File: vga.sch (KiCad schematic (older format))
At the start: 1 part

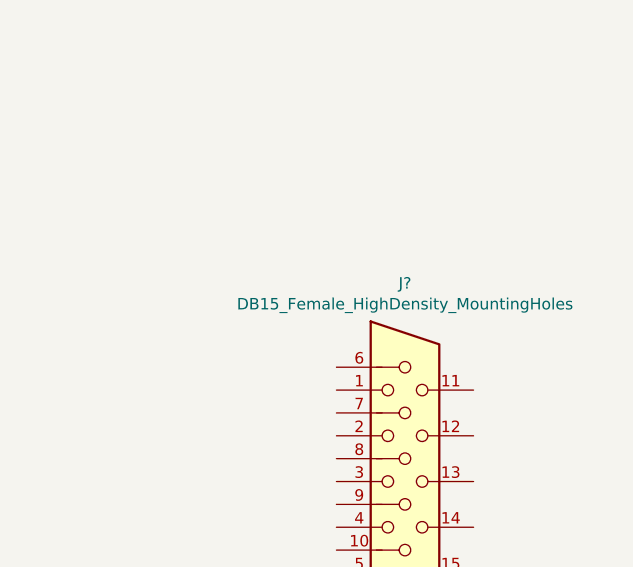
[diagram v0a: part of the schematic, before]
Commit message: Added some footprints. Basic board outline.
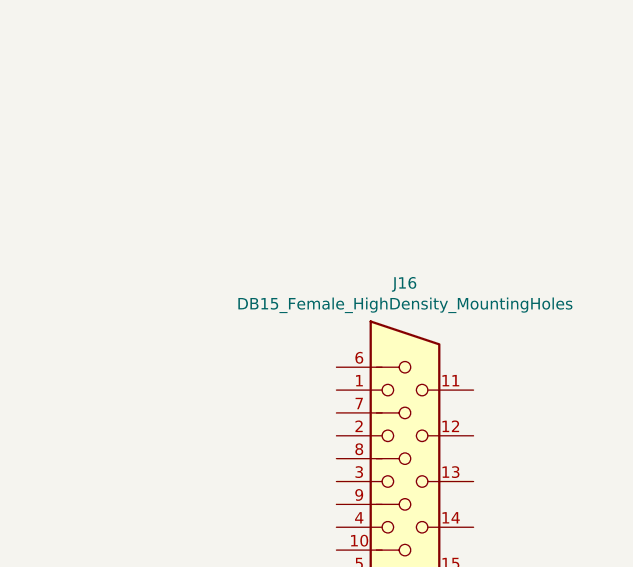
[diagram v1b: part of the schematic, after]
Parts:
- gave numbers to parts that had none: 1
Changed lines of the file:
@@
 $Descr A4 11693 8268
 encoding utf-8
-Sheet 5 11
+Sheet 11 11
 Title "Neotron 32K"
 Date "2019-12-08"
@@
 P 5500 4250
 AR Path="/5DF388AB" Ref="J?"  Part="1"
-AR Path="/5DF25A09/5DF388AB" Ref="J?"  Part="1"
-F 0 "J?" H 5500 5117 50  0000 C CNN
+AR Path="/5DF25A09/5DF388AB" Ref="J16"  Part="1"
+F 0 "J16" H 5500 5117 50  0000 C CNN
 F 1 "DB15_Female_HighDensity_MountingHoles" H 5500 5026 50  0000 C CNN
 F 2 "Connector_Dsub:DSUB-15-HD_Female_Horizontal_P2.29x1.98mm_EdgePinOffset3.03mm_Housed_MountingHolesOffset4.94mm" H 4550 4650 50  0001 C CNN

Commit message: Completed Power, SD, MIDI, Parallel and Joystick sheets.
Switch to sheet based 100x part numbering.
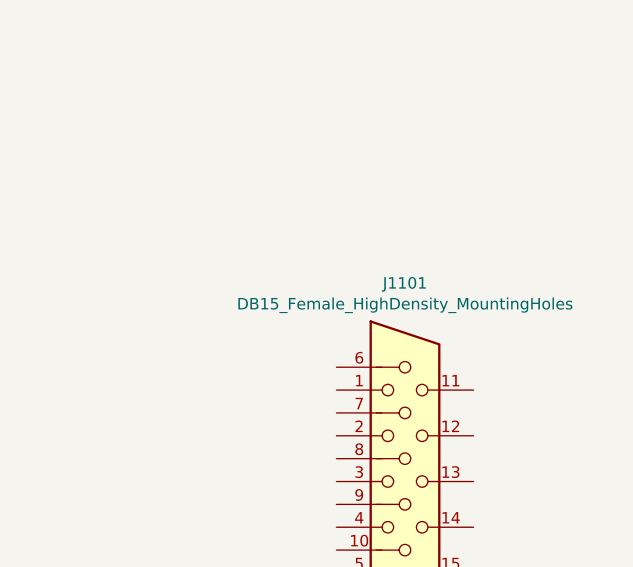
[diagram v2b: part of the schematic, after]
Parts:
- renumbered J16 to J1101
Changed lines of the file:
@@
 P 5500 4250
 AR Path="/5DF388AB" Ref="J?"  Part="1"
-AR Path="/5DF25A09/5DF388AB" Ref="J16"  Part="1"
-F 0 "J16" H 5500 5117 50  0000 C CNN
+AR Path="/5DF25A09/5DF388AB" Ref="J1101"  Part="1"
+F 0 "J1101" H 5500 5117 50  0000 C CNN
 F 1 "DB15_Female_HighDensity_MountingHoles" H 5500 5026 50  0000 C CNN
 F 2 "Connector_Dsub:DSUB-15-HD_Female_Horizontal_P2.29x1.98mm_EdgePinOffset3.03mm_Housed_MountingHolesOffset4.94mm" H 4550 4650 50  0001 C CNN

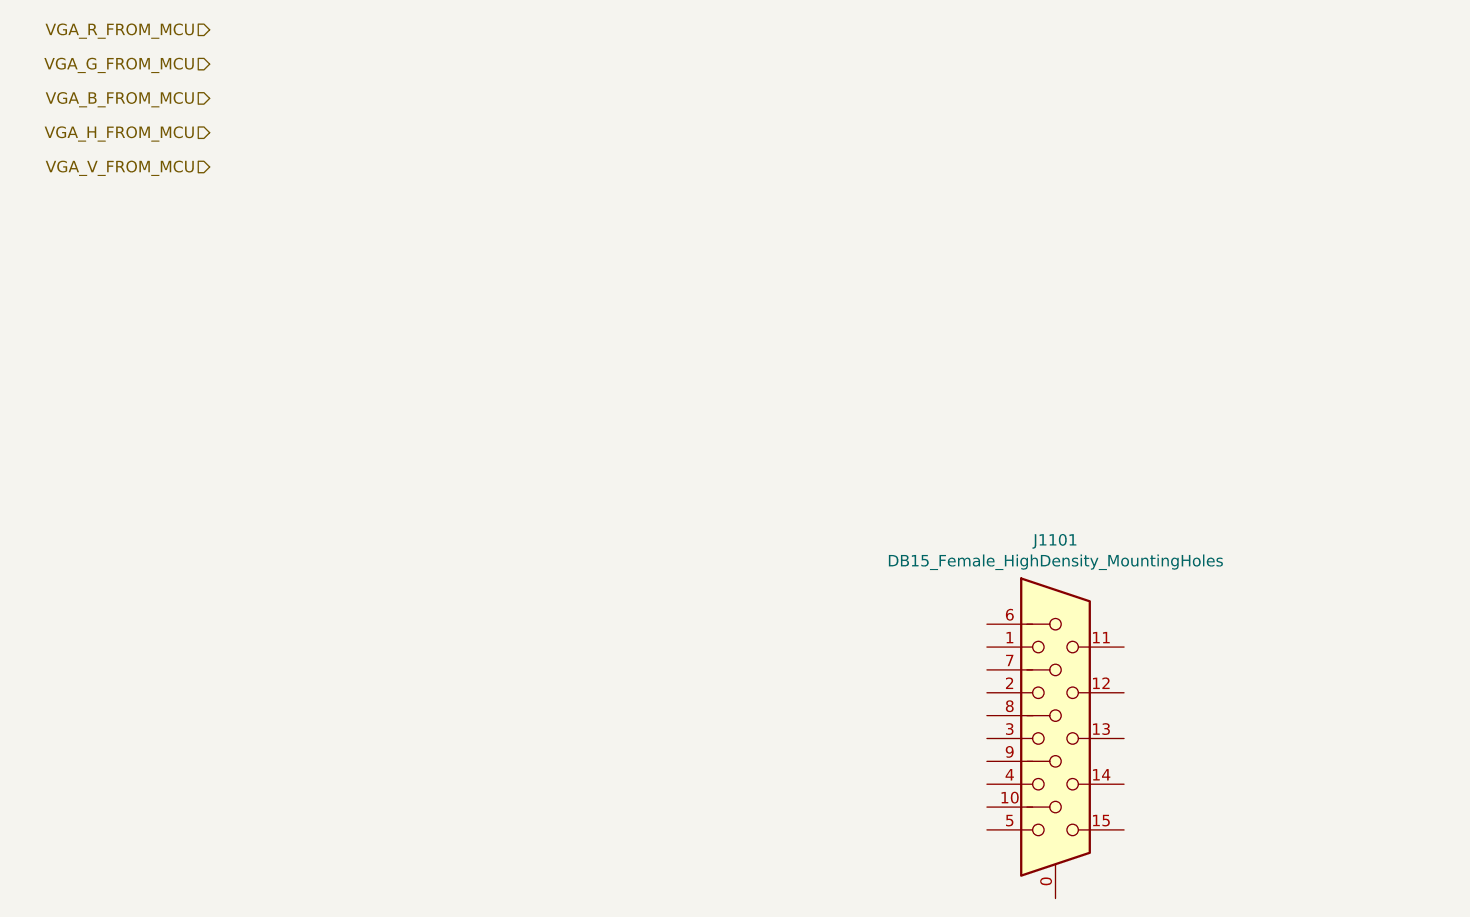
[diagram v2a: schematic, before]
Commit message: Schematic capture draft complete.
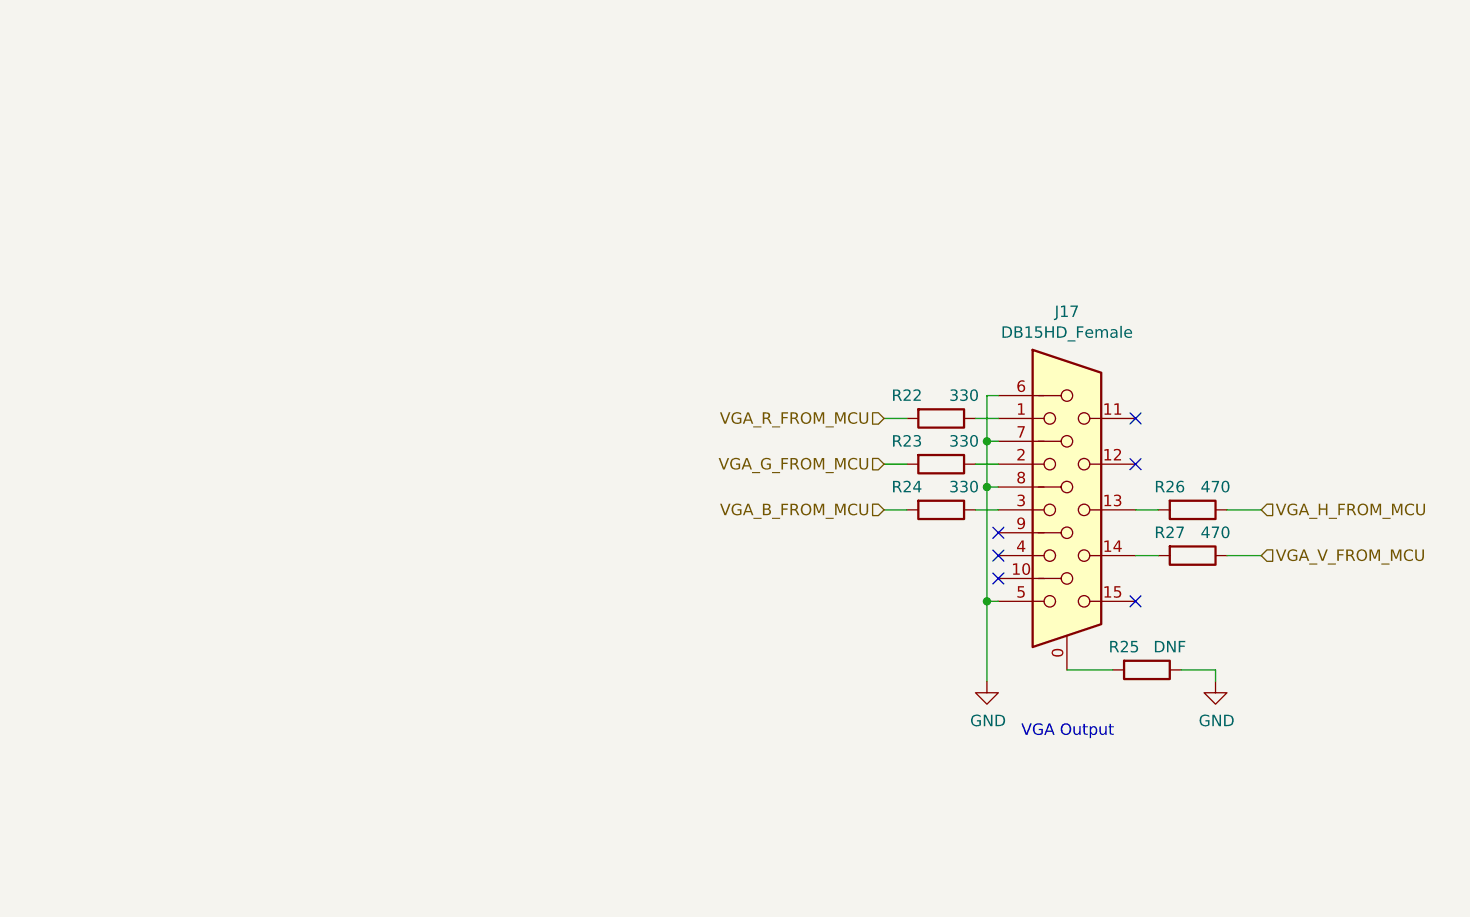
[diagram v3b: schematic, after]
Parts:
- added R22, R23, R24: 330, Resistor_THT:R_Axial_DIN0411_L9.9mm_D3.6mm_P12.70mm_Horizontal, symbol Device:R
- added R25: DNF, Resistor_THT:R_Axial_DIN0411_L9.9mm_D3.6mm_P12.70mm_Horizontal, symbol Device:R
- added R26, R27: 470, Resistor_THT:R_Axial_DIN0411_L9.9mm_D3.6mm_P12.70mm_Horizontal, symbol Device:R
- J17: renamed from J1101; value DB15_Female_HighDensity_MountingHoles -> DB15HD_Female; Digikey (none) -> 609-5180-ND
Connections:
- net VGA_B_FROM_MCU: now also R24.2
- net VGA_G_FROM_MCU: now also R23.2
- net VGA_H_FROM_MCU: now also R26.1
- net VGA_R_FROM_MCU: now also R22.2
- net VGA_V_FROM_MCU: now also R27.1
- net at J17.0: now also R25.2
- net at J17.1: now also R22.1
- net at J17.13: now also R26.2
- net at J17.14: now also R27.2
- net at J17.2: now also R23.1
- net at J17.3: now also R24.1
- net GND: now reaches J17.5
- net GND: now also J17.6, J17.7, J17.8, R25.1
- no-connect marks 0 -> 6
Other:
- note added: "VGA Output"
- moved on the sheet: J17
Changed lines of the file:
@@
 $Descr A4 11693 8268
 encoding utf-8
-Sheet 11 11
-Title "Neotron 32K"
-Date "2019-12-08"
-Rev "0.1"
-Comp "github.com/thejpster"
-Comment1 ""
-Comment2 ""
+Sheet 9 10
+Title "Neotron 32K Main PCB"
+Date "2019-12-15"
+Rev "0.5"
+Comp "github.com/neotron-compute/Neotron-32-Hardware"
+Comment1 "Copyright (c) Jonathan 'theJPster' Pallant"
+Comment2 "CC BY-SA 4.0"
 Comment3 ""
 Comment4 ""
@@
 L Connector:DB15_Female_HighDensity_MountingHoles J?
 U 1 1 5DF388AB
-P 5500 4250
+P 5550 3250
 AR Path="/5DF388AB" Ref="J?"  Part="1"
-AR Path="/5DF25A09/5DF388AB" Ref="J1101"  Part="1"
-F 0 "J1101" H 5500 5117 50  0000 C CNN
-F 1 "DB15_Female_HighDensity_MountingHoles" H 5500 5026 50  0000 C CNN
-F 2 "Connector_Dsub:DSUB-15-HD_Female_Horizontal_P2.29x1.98mm_EdgePinOffset3.03mm_Housed_MountingHolesOffset4.94mm" H 4550 4650 50  0001 C CNN
-F 3 " ~" H 4550 4650 50  0001 C CNN
-	1    5500 4250
+AR Path="/5DF25A09/5DF388AB" Ref="J17"  Part="1"
+F 0 "J17" H 5550 4117 50  0000 C CNN
+F 1 "DB15HD_Female" H 5550 4026 50  0000 C CNN
+F 2 "Connector_Dsub:DSUB-15-HD_Female_Horizontal_P2.29x1.98mm_EdgePinOffset3.03mm_Housed_MountingHolesOffset4.94mm" H 4600 3650 50  0001 C CNN
+F 3 "https://www.amphenol-icc.com/media/wysiwyg/files/drawing/c-cd-0012.pdf" H 4600 3650 50  0001 C CNN
+F 4 "609-5180-ND" H 5550 3250 50  0001 C CNN "Digikey"
+	1    5550 3250
 	1    0    0    -1
 $EndComp
-Text HLabel 1800 1150 0    50   Input ~ 0
+Text HLabel 4750 2850 0    50   Input ~ 0
 VGA_R_FROM_MCU
-Text HLabel 1800 1300 0    50   Input ~ 0
+Text HLabel 4750 3050 0    50   Input ~ 0
 VGA_G_FROM_MCU
-Text HLabel 1800 1450 0    50   Input ~ 0
+Text HLabel 4750 3250 0    50   Input ~ 0
 VGA_B_FROM_MCU
-Text HLabel 1800 1600 0    50   Input ~ 0
+Text HLabel 6400 3250 2    50   Input ~ 0
 VGA_H_FROM_MCU
-Text HLabel 1800 1750 0    50   Input ~ 0
+Text HLabel 6400 3450 2    50   Input ~ 0
 VGA_V_FROM_MCU
+$Comp
+L Device:R R27
+U 1 1 5E020EF6
+P 6100 3450
+F 0 "R27" V 6000 3350 50  0000 C CNN
+F 1 "470" V 6000 3550 50  0000 C CNN
+F 2 "Resistor_THT:R_Axial_DIN0411_L9.9mm_D3.6mm_P12.70mm_Horizontal" V 6030 3450 50  0001 C CNN
+F 3 "~" H 6100 3450 50  0001 C CNN
+	1    6100 3450
+	0    1    1    0
+$EndComp
+$Comp
+L Device:R R26
+U 1 1 5E02143C
+P 6100 3250
+F 0 "R26" V 6000 3150 50  0000 C CNN
+F 1 "470" V 6000 3350 50  0000 C CNN
+F 2 "Resistor_THT:R_Axial_DIN0411_L9.9mm_D3.6mm_P12.70mm_Horizontal" V 6030 3250 50  0001 C CNN
+F 3 "~" H 6100 3250 50  0001 C CNN
+	1    6100 3250
+	0    1    1    0
+$EndComp
+$Comp
+L Device:R R22
+U 1 1 5E021698
+P 5000 2850
+F 0 "R22" V 4900 2700 50  0000 C CNN
+F 1 "330" V 4900 2950 50  0000 C CNN
+F 2 "Resistor_THT:R_Axial_DIN0411_L9.9mm_D3.6mm_P12.70mm_Horizontal" V 4930 2850 50  0001 C CNN
+F 3 "~" H 5000 2850 50  0001 C CNN
+	1    5000 2850
+	0    1    1    0
+$EndComp
+$Comp
+L Device:R R23
+U 1 1 5E021BC3
+P 5000 3050
+F 0 "R23" V 4900 2900 50  0000 C CNN
+F 1 "330" V 4900 3150 50  0000 C CNN
+F 2 "Resistor_THT:R_Axial_DIN0411_L9.9mm_D3.6mm_P12.70mm_Horizontal" V 4930 3050 50  0001 C CNN
+F 3 "~" H 5000 3050 50  0001 C CNN
+	1    5000 3050
+	0    1    1    0
+$EndComp
+$Comp
+L Device:R R24
+U 1 1 5E021E5E
+P 5000 3250
+F 0 "R24" V 4900 3100 50  0000 C CNN
+F 1 "330" V 4900 3350 50  0000 C CNN
+F 2 "Resistor_THT:R_Axial_DIN0411_L9.9mm_D3.6mm_P12.70mm_Horizontal" V 4930 3250 50  0001 C CNN
+F 3 "~" H 5000 3250 50  0001 C CNN
+	1    5000 3250
+	0    1    1    0
+$EndComp
+Wire Wire Line
+	4750 2850 4850 2850
+Wire Wire Line
+	4750 3050 4850 3050
+Wire Wire Line
+	4750 3250 4850 3250
+Wire Wire Line
+	5150 2850 5250 2850
+Wire Wire Line
+	5150 3050 5250 3050
+Wire Wire Line
+	5150 3250 5250 3250
+Wire Wire Line
+	5850 3250 5950 3250
+Wire Wire Line
+	6250 3250 6400 3250
+Wire Wire Line
+	6250 3450 6400 3450
+Wire Wire Line
+	5850 3450 5950 3450
+NoConn ~ 5850 3650
+NoConn ~ 5250 3550
+NoConn ~ 5250 3450
+NoConn ~ 5250 3350
+NoConn ~ 5850 2850
+NoConn ~ 5850 3050
+Wire Wire Line
+	5250 2750 5200 2750
+Wire Wire Line
+	5200 2750 5200 2950
+Wire Wire Line
+	5200 2950 5250 2950
+Connection ~ 5200 2950
+Wire Wire Line
+	5200 2950 5200 3150
+Wire Wire Line
+	5200 3150 5250 3150
+Connection ~ 5200 3150
+Wire Wire Line
+	5200 3150 5200 3650
+Wire Wire Line
+	5200 3650 5250 3650
+Connection ~ 5200 3650
+$Comp
+L power:GND #PWR066
+U 1 1 5E02516A
+P 5200 4000
+F 0 "#PWR066" H 5200 3750 50  0001 C CNN
+F 1 "GND" H 5205 3827 50  0000 C CNN
+F 2 "" H 5200 4000 50  0001 C CNN
+F 3 "" H 5200 4000 50  0001 C CNN
+	1    5200 4000
+	1    0    0    -1
+$EndComp
+Text Notes 5350 4250 0    50   ~ 0
+VGA Output
+$Comp
+L Device:R R25
+U 1 1 5E3BC4C1
+P 5900 3950
+F 0 "R25" V 5800 3850 50  0000 C CNN
+F 1 "DNF" V 5800 4050 50  0000 C CNN
+F 2 "Resistor_THT:R_Axial_DIN0411_L9.9mm_D3.6mm_P12.70mm_Horizontal" V 5830 3950 50  0001 C CNN
+F 3 "~" H 5900 3950 50  0001 C CNN
+	1    5900 3950
+	0    1    1    0
+$EndComp
+$Comp
+L power:GND #PWR067
+U 1 1 5E3BC797
+P 6200 4000
+F 0 "#PWR067" H 6200 3750 50  0001 C CNN
+F 1 "GND" H 6205 3827 50  0000 C CNN
+F 2 "" H 6200 4000 50  0001 C CNN
+F 3 "" H 6200 4000 50  0001 C CNN
+	1    6200 4000
+	1    0    0    -1
+$EndComp
+Wire Wire Line
+	5550 3950 5750 3950
+Wire Wire Line
+	6050 3950 6200 3950
+Wire Wire Line
+	6200 3950 6200 4000
+Wire Wire Line
+	5200 3650 5200 4000
 $EndSCHEMATC

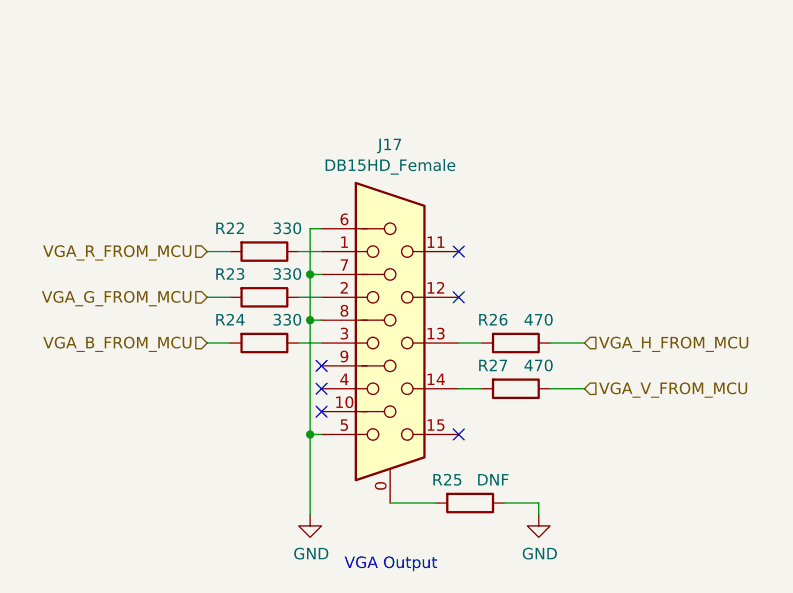
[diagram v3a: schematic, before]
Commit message: Tidied up Atmega power. Added page titles.
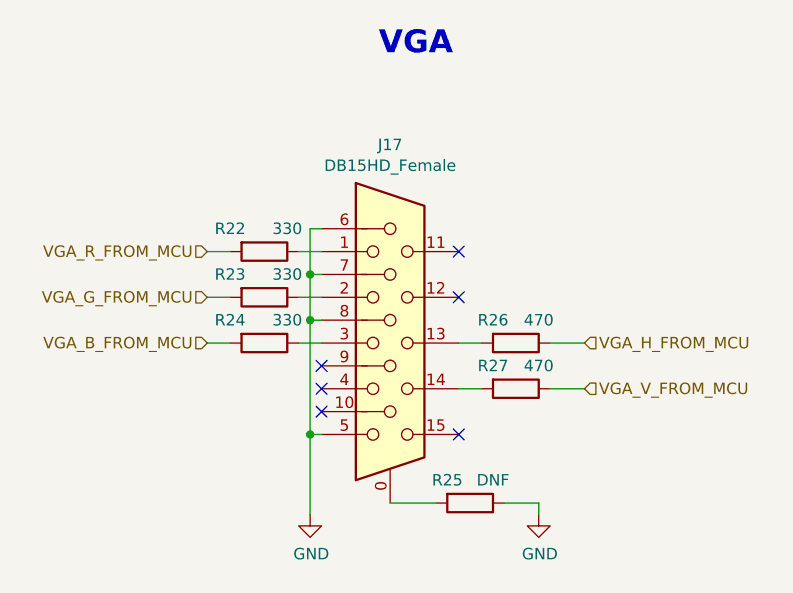
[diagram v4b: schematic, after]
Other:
- note added: "VGA"
- note removed: "VGA Output"
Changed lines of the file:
@@
 Sheet 9 10
 Title "Neotron 32K Main PCB"
-Date "2019-12-15"
-Rev "0.5"
+Date "2019-12-16"
+Rev "0.6"
 Comp "github.com/neotron-compute/Neotron-32-Hardware"
 Comment1 "Copyright (c) Jonathan 'theJPster' Pallant"
@@
 	1    0    0    -1
 $EndComp
-Text Notes 5350 4250 0    50   ~ 0
-VGA Output
 $Comp
 L Device:R R25
@@
 Wire Wire Line
 	5200 3650 5200 4000
+Text Notes 5500 2000 0    100  ~ 20
+VGA
 $EndSCHEMATC

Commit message: Updated footprints: ) Swapped RS-232 DE9 for IDC header. ) Large caps are radial electrolytics. ) Made resistors a little smaller.
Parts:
- R22, R23, R24, R25, R26, R27: footprint Resistor_THT:R_Axial_DIN0411_L9.9mm_D3.6mm_P12.70mm_Horizontal -> Resistor_THT:R_Axial_DIN0207_L6.3mm_D2.5mm_P10.16mm_Horizontal
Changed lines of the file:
@@
 F 0 "R27" V 6000 3350 50  0000 C CNN
 F 1 "470" V 6000 3550 50  0000 C CNN
-F 2 "Resistor_THT:R_Axial_DIN0411_L9.9mm_D3.6mm_P12.70mm_Horizontal" V 6030 3450 50  0001 C CNN
+F 2 "Resistor_THT:R_Axial_DIN0207_L6.3mm_D2.5mm_P10.16mm_Horizontal" V 6030 3450 50  0001 C CNN
 F 3 "~" H 6100 3450 50  0001 C CNN
 	1    6100 3450
@@
 F 0 "R26" V 6000 3150 50  0000 C CNN
 F 1 "470" V 6000 3350 50  0000 C CNN
-F 2 "Resistor_THT:R_Axial_DIN0411_L9.9mm_D3.6mm_P12.70mm_Horizontal" V 6030 3250 50  0001 C CNN
+F 2 "Resistor_THT:R_Axial_DIN0207_L6.3mm_D2.5mm_P10.16mm_Horizontal" V 6030 3250 50  0001 C CNN
 F 3 "~" H 6100 3250 50  0001 C CNN
 	1    6100 3250
@@
 F 0 "R22" V 4900 2700 50  0000 C CNN
 F 1 "330" V 4900 2950 50  0000 C CNN
-F 2 "Resistor_THT:R_Axial_DIN0411_L9.9mm_D3.6mm_P12.70mm_Horizontal" V 4930 2850 50  0001 C CNN
+F 2 "Resistor_THT:R_Axial_DIN0207_L6.3mm_D2.5mm_P10.16mm_Horizontal" V 4930 2850 50  0001 C CNN
 F 3 "~" H 5000 2850 50  0001 C CNN
 	1    5000 2850
@@
 F 0 "R23" V 4900 2900 50  0000 C CNN
 F 1 "330" V 4900 3150 50  0000 C CNN
-F 2 "Resistor_THT:R_Axial_DIN0411_L9.9mm_D3.6mm_P12.70mm_Horizontal" V 4930 3050 50  0001 C CNN
+F 2 "Resistor_THT:R_Axial_DIN0207_L6.3mm_D2.5mm_P10.16mm_Horizontal" V 4930 3050 50  0001 C CNN
 F 3 "~" H 5000 3050 50  0001 C CNN
 	1    5000 3050
@@
 F 0 "R24" V 4900 3100 50  0000 C CNN
 F 1 "330" V 4900 3350 50  0000 C CNN
-F 2 "Resistor_THT:R_Axial_DIN0411_L9.9mm_D3.6mm_P12.70mm_Horizontal" V 4930 3250 50  0001 C CNN
+F 2 "Resistor_THT:R_Axial_DIN0207_L6.3mm_D2.5mm_P10.16mm_Horizontal" V 4930 3250 50  0001 C CNN
 F 3 "~" H 5000 3250 50  0001 C CNN
 	1    5000 3250
@@
 F 0 "R25" V 5800 3850 50  0000 C CNN
 F 1 "DNF" V 5800 4050 50  0000 C CNN
-F 2 "Resistor_THT:R_Axial_DIN0411_L9.9mm_D3.6mm_P12.70mm_Horizontal" V 5830 3950 50  0001 C CNN
+F 2 "Resistor_THT:R_Axial_DIN0207_L6.3mm_D2.5mm_P10.16mm_Horizontal" V 5830 3950 50  0001 C CNN
 F 3 "~" H 5900 3950 50  0001 C CNN
 	1    5900 3950
